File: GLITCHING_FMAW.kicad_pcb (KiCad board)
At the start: 4 copper layers, 49 x 49 mm, 72 parts, among them J1 USB_C_Receptacle_USB2.0_16P, J2 AIN, J3 GLITCH, J4 ANA1, J5 ANA2, J6 ANA3, J7 GND, Q2 IRLB8721PBF, U1 TLV76133, U2 TLV76133, U3 LM358, U4 RP2040, U5 W25Q128JVS, U6 MS9280, Y1 12MHz

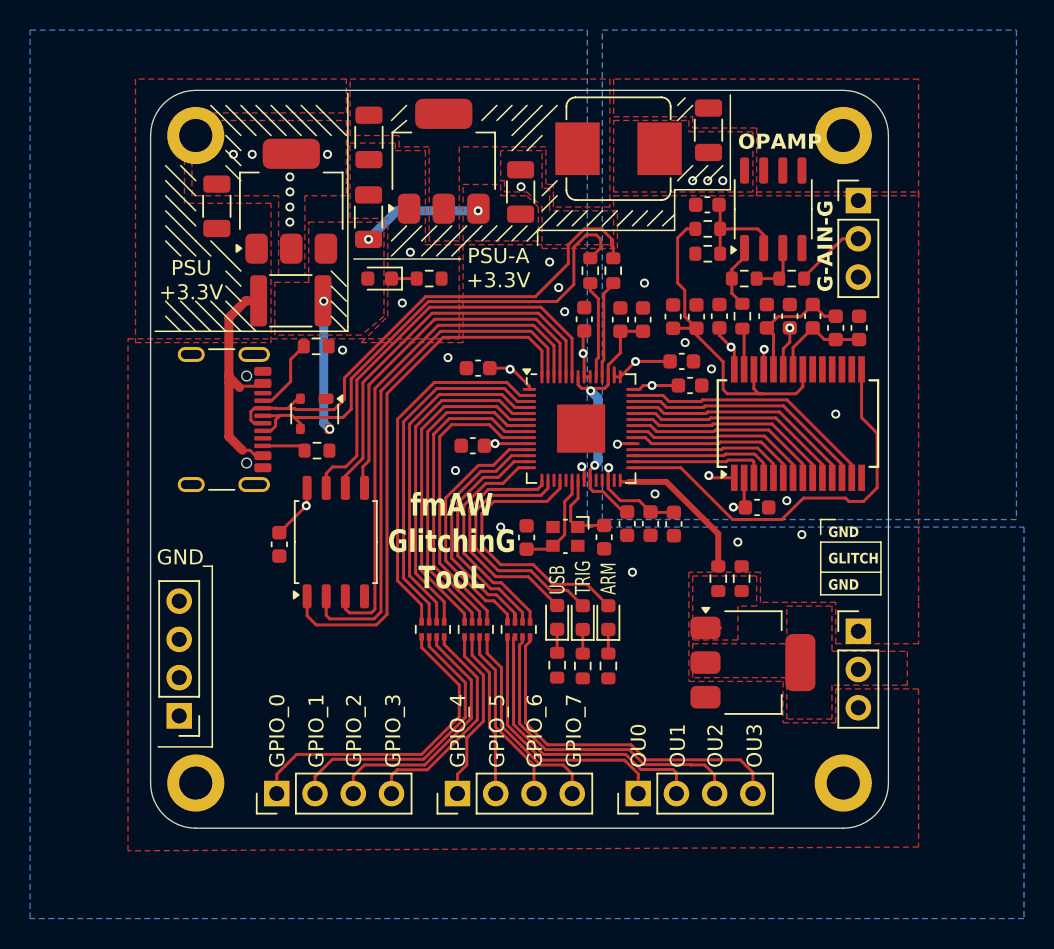
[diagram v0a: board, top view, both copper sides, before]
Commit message: minor changes to convert into 2 layers board
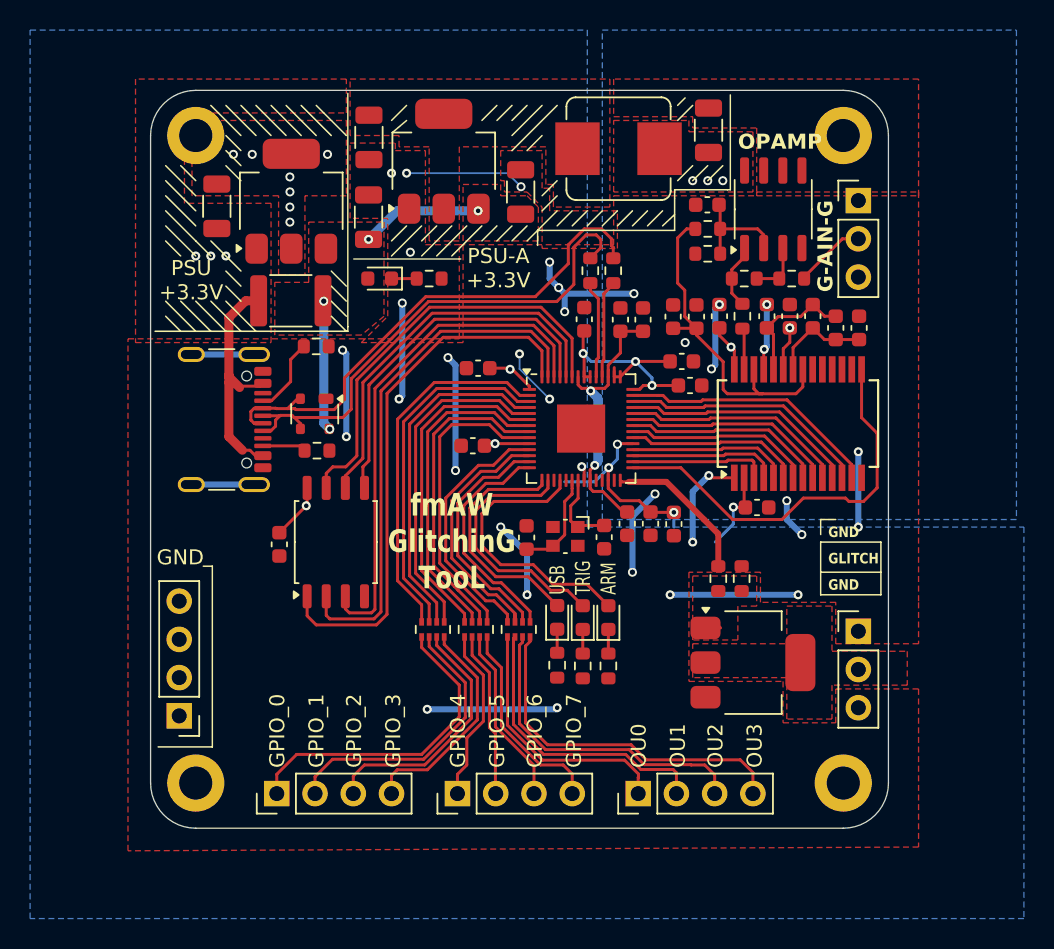
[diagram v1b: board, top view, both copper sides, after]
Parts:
- C17, C18: value tbd -> 8pF
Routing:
- net GND: track 3.10 -> 99.9 mm, vias 21 -> 38
- net +3.3V: track 33.3 -> 48.0 mm, vias 17 -> 18
- added copper zone on B.Cu, net +3.3V
- removed copper zone on In1.Cu, net +3.3V
- removed copper zone on B.Cu, net GND
- removed copper zone on In2.Cu, net GND
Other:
- copper layers 4 -> 2

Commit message: v1-layer
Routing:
- net Net-(F1-Pad1): track 16.7 -> 15.6 mm
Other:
- board text added: "HW HACKING ES Spec. Edition"
- board text added: "Mod from tjclement"
- board text added: "fmaw GlitchinG"
- board text removed: "COPY of BOLT Glitching by tjclement"
- board text removed: "fmAW GlitchinG TooL"
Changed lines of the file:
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@@
 			(drillshape 0)
 			(scaleselection 1)
-			(outputdirectory "FABRICATION/gerber/")
+			(outputdirectory "FABRICATION/gerber_2layer/")
 		)
 	)
@@
 			)
 		)
+		(model "${KICAD8_3DMODEL_DIR}/Package_SO.3dshapes/SO-8_3.9x4.9mm_P1.27mm.step"
+			(offset
+				(xyz 0 0 0)
+			)
+			(scale
+				(xyz 1 1 1)
+			)
+			(rotate
+				(xyz 0 0 0)
+			)
+		)
 	)
 	(footprint "Package_SO:SO-8_3.9x4.9mm_P1.27mm"
@@
 			)
 		)
+		(model "${KICAD8_3DMODEL_DIR}/Fuse.3dshapes/Fuse_1210_3225Metric.step"
+			(offset
+				(xyz 0 0 0)
+			)
+			(scale
+				(xyz 1.3 1.3 1)
+			)
+			(rotate
+				(xyz 0 0 0)
+			)
+		)
 	)
 	(footprint "Capacitor_SMD:C_0603_1608Metric"
@@
 		(layer "Edge.Cuts")
 	)
-	(gr_text "COPY of BOLT\nGlitching\nby tjclement"
+	(gr_text "Mod from \ntjclement"
 		(at 54 66.5 0)
 		(layer "B.SilkS" knockout)
@@
 				(bold yes)
 			)
-			(justify bottom)
+			(justify bottom mirror)
 		)
 	)
@@
 		)
 	)
-	(gr_text "fmAW\nGlitchinG\nTooL"
-		(at 50 57.25 0)
-		(layer "F.SilkS" knockout)
+	(gr_text "fmaw\nGlitchinG"
+		(at 34.4 63 0)
+		(layer "F.SilkS")
 		(effects
 			(font
@@
 				(bold yes)
 			)
-			(justify bottom)
+			(justify left bottom)
 		)
 	)
@@
 		)
 	)
+	(gr_text "HW HACKING ES\nSpec. Edition"
+		(at 49.1 56.8 90)
+		(layer "F.SilkS" knockout)
+		(effects
+			(font
+				(size 1 1.5)
+				(thickness 0.25)
+				(bold yes)
+			)
+			(justify left bottom)
+		)
+	)
 	(dimension
 		(type aligned)
@@
 	)
 	(segment
-		(start 36.1 47.9)
-		(end 36.6 47.9)
+		(start 36.659594 43.645)
+		(end 36.255 43.645)
 		(width 0.2)
 		(layer "F.Cu")
@@
 	)
 	(segment
-		(start 35.2 43.4)
-		(end 35.2 42.9)
-		(width 0.6)
+		(start 36.255 43.645)
+		(end 36.048299 43.851701)
+		(width 0.2)
 		(layer "F.Cu")
 		(net 19)
 	)
 	(segment
-		(start 37.27 43.645)
-		(end 35.445 43.645)
-		(width 0.2)
+		(start 35.6 43.851701)
+		(end 35.11 43.361701)
+		(width 1.2)
 		(layer "F.Cu")
 		(net 19)
 	)
 	(segment
-		(start 36.6 47.9)
-		(end 36.96 48.26)
+		(start 35.11 43.361701)
+		(end 35.11 39.1825)
+		(width 1.2)
+		(layer "F.Cu")
+		(net 19)
+	)
+	(segment
+		(start 36.1 47.6)
+		(end 36.3 47.6)
 		(width 0.2)
 		(layer "F.Cu")
@@
 	)
 	(segment
-		(start 35.2 43.027437)
-		(end 35.908782 43.736219)
-		(width 0.6)
+		(start 37.455 43.46)
+		(end 36.844594 43.46)
+		(width 0.2)
 		(layer "F.Cu")
 		(net 19)
@@
 	)
 	(segment
-		(start 35.2 42.9)
-		(end 35.2 43.027437)
+		(start 36.3175 37.975)
+		(end 37.175 37.975)
 		(width 0.6)
 		(layer "F.Cu")
@@
 	)
 	(segment
-		(start 36.3175 37.975)
-		(end 37.175 37.975)
-		(width 0.6)
+		(start 35.6 43.851701)
+		(end 35.6 44.045001)
+		(width 0.2)
 		(layer "F.Cu")
 		(net 19)
 	)
 	(segment
-		(start 37.455 43.46)
-		(end 37.27 43.645)
+		(start 36.048299 43.851701)
+		(end 35.6 43.851701)
 		(width 0.2)
 		(layer "F.Cu")
@@
 	)
 	(segment
-		(start 36.96 48.26)
-		(end 37.455 48.26)
+		(start 36.844594 43.46)
+		(end 36.659594 43.645)
 		(width 0.2)
 		(layer "F.Cu")
@@
 	)
 	(segment
-		(start 35.2 42.9)
-		(end 35.2 39.0925)
-		(width 0.6)
+		(start 35.6 47.1)
+		(end 35.6 43.851701)
+		(width 1.2)
 		(layer "F.Cu")
 		(net 19)
 	)
 	(segment
-		(start 35.2 39.0925)
+		(start 35.11 39.1825)
 		(end 36.3175 37.975)
-		(width 0.6)
+		(width 1.2)
 		(layer "F.Cu")
 		(net 19)
 	)
 	(segment
-		(start 35.2 47)
-		(end 35.2 43.4)
-		(width 0.6)
+		(start 36.96 48.26)
+		(end 37.455 48.26)
+		(width 0.2)
 		(layer "F.Cu")
 		(net 19)
 	)
 	(segment
-		(start 36.1 47.9)
-		(end 35.2 47)
-		(width 0.6)
+		(start 36.1 47.6)
+		(end 35.6 47.1)
+		(width 1.2)
+		(layer "F.Cu")
+		(net 19)
+	)
+	(segment
+		(start 36.3 47.6)
+		(end 36.96 48.26)
+		(width 0.2)
 		(layer "F.Cu")
 		(net 19)
